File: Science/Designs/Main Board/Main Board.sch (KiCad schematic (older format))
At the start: 49 parts

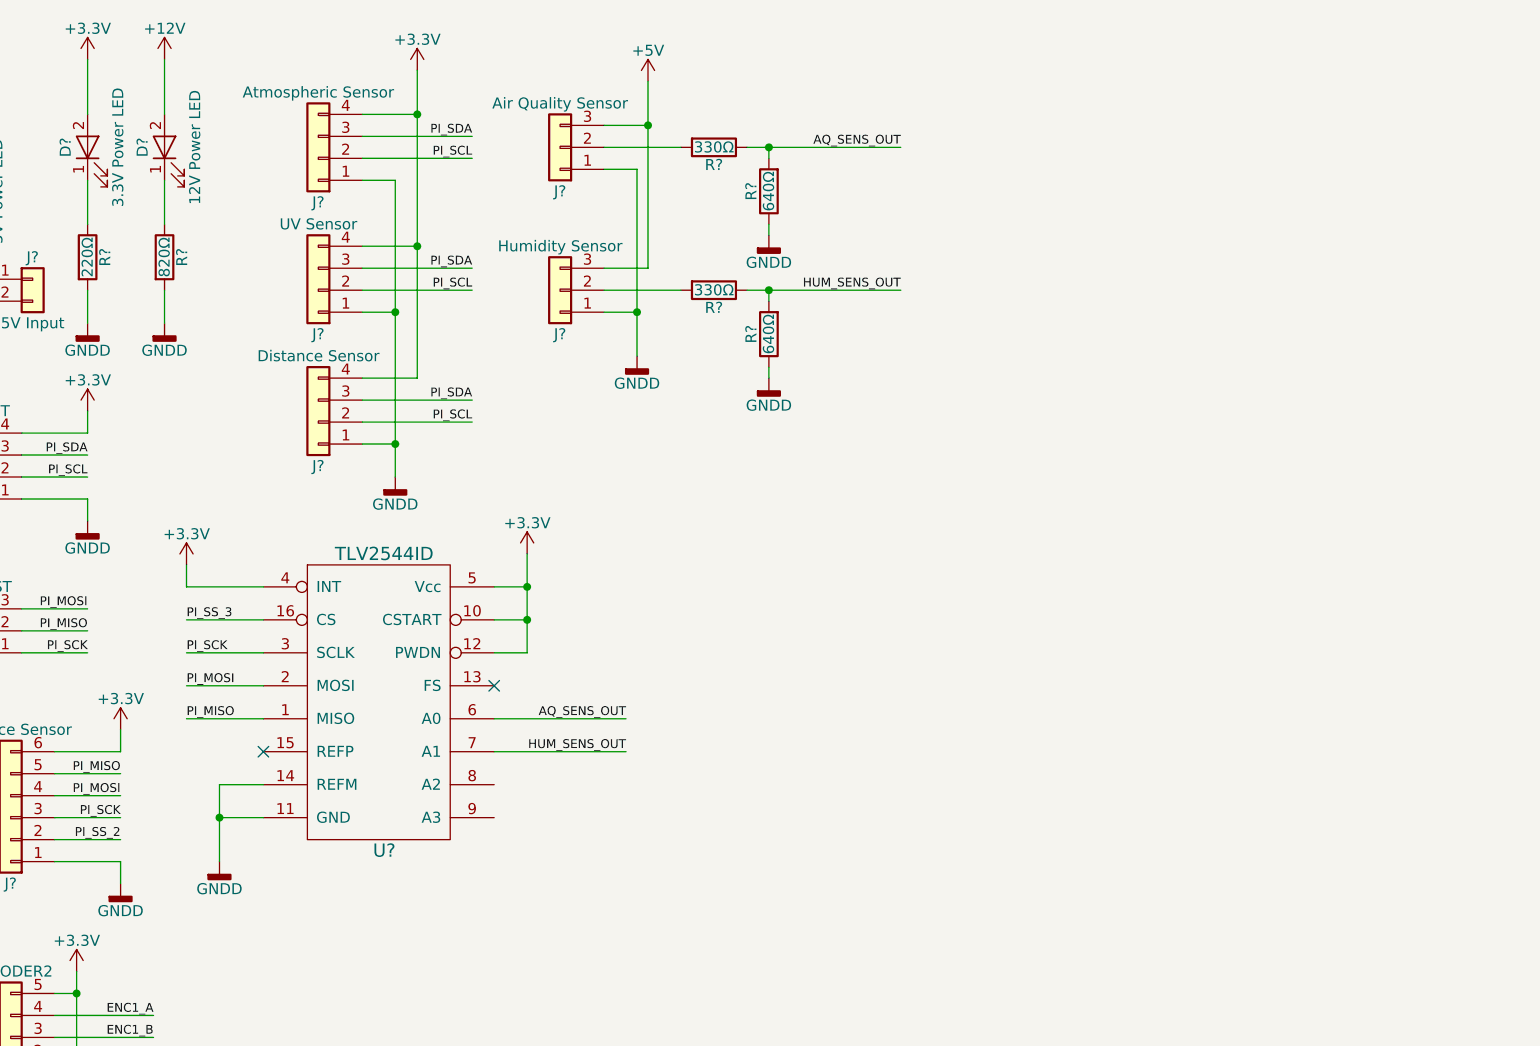
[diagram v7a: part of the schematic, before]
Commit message: Aded PWM device to schematic
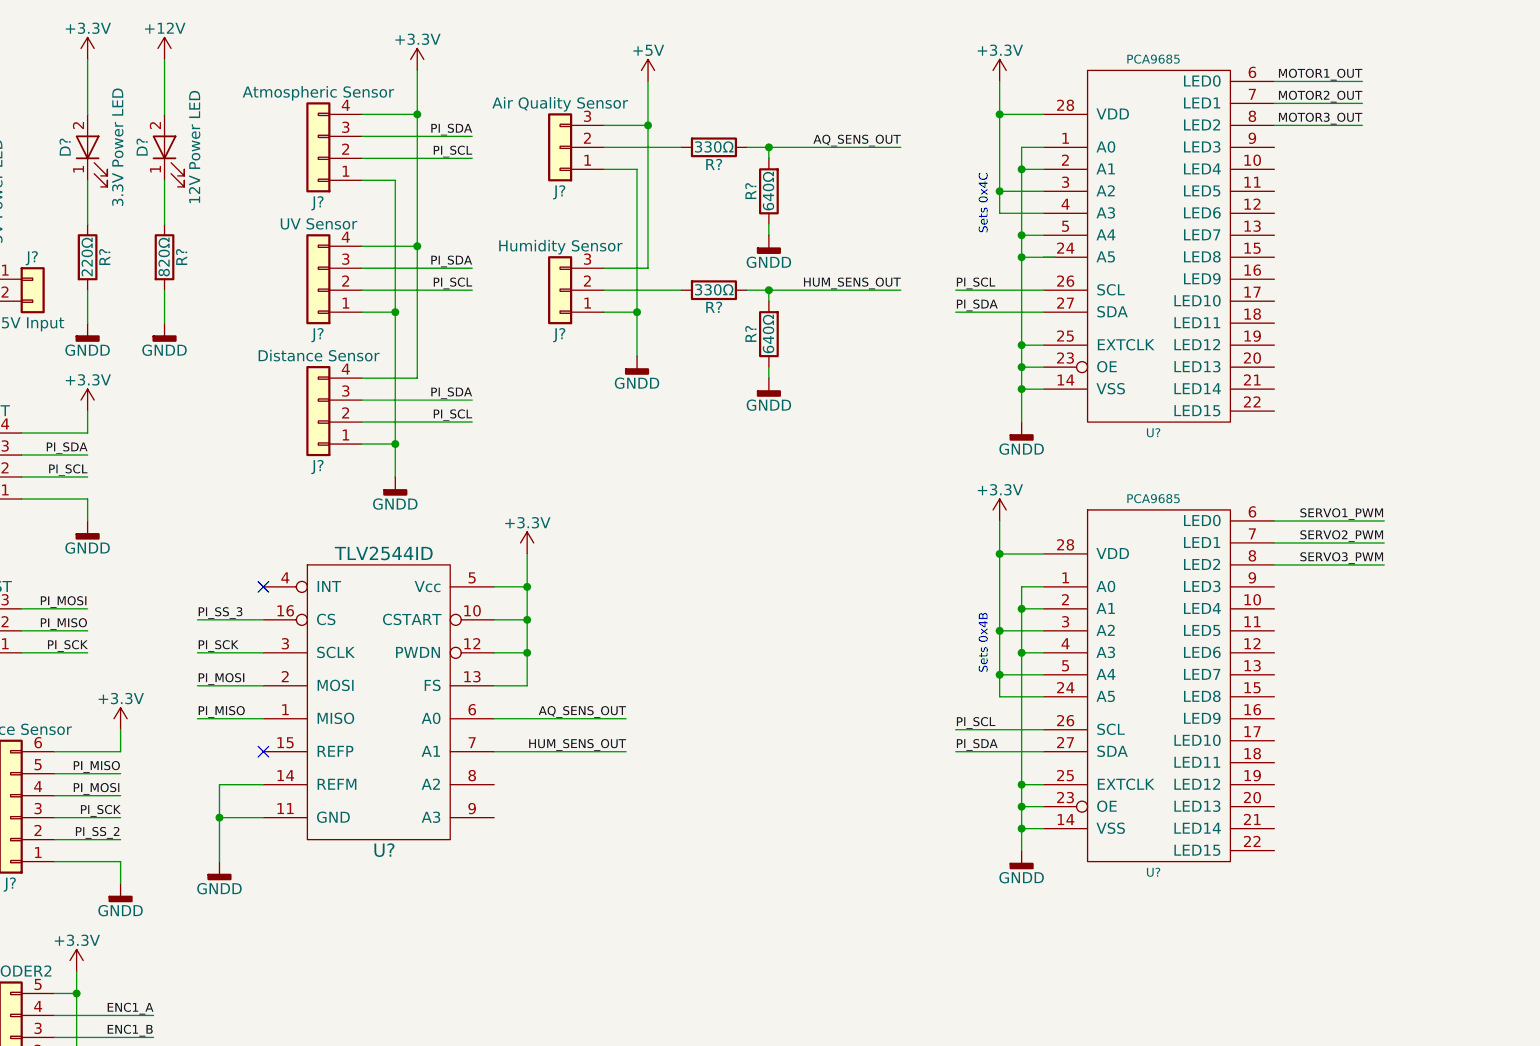
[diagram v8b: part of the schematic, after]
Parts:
- removed U?: TLV2544ID, symbol TLV2544ID
- added U?: TLV2544ID, symbol TLV2544ID
- added U? (x2): PCA9685, symbol PCA9685
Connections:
- net +3V3: now also U?.10 (CSTART), U?.12 (PWDN), U?.13 (FS), U?.24 (A5), U?.28 (VDD), U?.28 (VDD), U?.3 (A2), U?.3 (A2), U?.4 (A3), U?.5 (A4), U?.5 (Vcc)
- net AQ_SENS_OUT: now also U?.6 (A0)
- net GNDD: now also U?.1 (A0), U?.1 (A0), U?.11 (GND), U?.14 (REFM), U?.14 (VSS), U?.14 (VSS), U?.2 (A1), U?.2 (A1), U?.23 (OE), U?.23 (OE), U?.25 (EXTCLK), U?.25 (EXTCLK), U?.4 (A3), U?.5 (A4)
- net HUM_SENS_OUT: now also U?.7 (A1)
- net MOTOR1_OUT: now also U?.6 (LED0)
- net MOTOR2_OUT: now also U?.7 (LED1)
- net MOTOR3_OUT: now also U?.8 (LED2)
- net PI_MISO: now also U?.1 (MISO)
- net PI_MOSI: now also U?.2 (MOSI)
- net PI_SCK: now also U?.3 (SCLK)
- net PI_SCL: now also U?.26 (SCL), U?.26 (SCL)
- net PI_SDA: now also U?.27 (SDA), U?.27 (SDA)
- net PI_SS_3: now also U?.16 (CS)
- net SERVO1_PWM: now also U?.6 (LED0)
- net SERVO2_PWM: now also U?.7 (LED1)
- net SERVO3_PWM: now also U?.8 (LED2)
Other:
- note added: "Sets 0x4B"
- note added: "Sets 0x4C"
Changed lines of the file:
@@
-$EndComp
-$Comp
-L TLV2544ID U?
-U 1 1 5A52817B
-P 2500 3800
-F 0 "U?" H 2500 3300 60  0000 C CNN
-F 1 "TLV2544ID" H 2500 4650 60  0000 C CNN
-F 2 "" H 2500 4650 60  0001 C CNN
-F 3 "" H 2500 4650 60  0001 C CNN
-	1    2500 3800
-	1    0    0    -1
 $EndComp
 $Comp
@@
 	1    0    0    -1
 $EndComp
-NoConn ~ 3000 3550
 NoConn ~ 1950 3850
-Text Label 1600 3400 0    40   ~ 0
+Text Label 1650 3400 0    40   ~ 0
 PI_SCK
-Text Label 1600 3550 0    40   ~ 0
+Text Label 1650 3550 0    40   ~ 0
 PI_MOSI
-Text Label 1600 3700 0    40   ~ 0
+Text Label 1650 3700 0    40   ~ 0
 PI_MISO
 $Comp
@@
 	3000 3100 3150 3100
 Wire Wire Line
-	3150 2950 3150 3400
+	3150 2950 3150 3550
 Wire Wire Line
 	1950 4150 1750 4150
@@
 Connection ~ 1750 4150
 Wire Wire Line
-	1950 3700 1600 3700
-Wire Wire Line
-	1950 3550 1600 3550
-Wire Wire Line
-	1950 3400 1600 3400
-Wire Wire Line
-	1950 3250 1600 3250
+	1950 3700 1650 3700
+Wire Wire Line
+	1950 3550 1650 3550
+Wire Wire Line
+	1950 3400 1650 3400
+Wire Wire Line
+	1950 3250 1650 3250
 Wire Wire Line
 	4150 1100 4850 1100
@@
 Text Label 9800 2300 0    40   ~ 0
 PI_SS_3
-Text Label 1600 3250 0    40   ~ 0
+Text Label 1650 3250 0    40   ~ 0
 PI_SS_3
-Wire Wire Line
-	1950 3100 1600 3100
-Wire Wire Line
-	1600 3100 1600 3000
+$Comp
+L TLV2544ID U?
+U 1 1 5A5313CE
+P 2500 3800
+F 0 "U?" H 2500 3300 60  0000 C CNN
+F 1 "TLV2544ID" H 2500 4650 60  0000 C CNN
+F 2 "" H 2500 4650 60  0001 C CNN
+F 3 "" H 2500 4650 60  0001 C CNN
+	1    2500 3800
+	1    0    0    -1
+$EndComp
+Wire Wire Line
+	3150 3550 3000 3550
+Connection ~ 3150 3400
+NoConn ~ 1950 3100
+$Comp
+L PCA9685 U?
+U 1 1 5A534637
+P 6000 3350
+F 0 "U?" H 6000 2300 40  0000 C CNN
+F 1 "PCA9685" H 6000 4000 40  0000 C CNN
+F 2 "" H 6000 2300 40  0001 C CNN
+F 3 "" H 6000 2300 40  0001 C CNN
+	1    6000 3350
+	1    0    0    -1
+$EndComp
+$Comp
+L PCA9685 U?
+U 1 1 5A5346EA
+P 6000 1350
+F 0 "U?" H 6000 300 40  0000 C CNN
+F 1 "PCA9685" H 6000 2000 40  0000 C CNN
+F 2 "" H 6000 300 40  0001 C CNN
+F 3 "" H 6000 300 40  0001 C CNN
+	1    6000 1350
+	1    0    0    -1
+$EndComp
+Wire Wire Line
+	5500 2000 5400 2000
+Wire Wire Line
+	5400 1100 5400 2350
+Wire Wire Line
+	5500 2200 5400 2200
+Connection ~ 5400 2200
+Wire Wire Line
+	5500 2100 5400 2100
+Connection ~ 5400 2100
+$Comp
+L GNDD #PWR?
+U 1 1 5A534CEC
+P 5400 2350
+F 0 "#PWR?" H 5400 2100 50  0001 C CNN
+F 1 "GNDD" H 5400 2225 50  0000 C CNN
+F 2 "" H 5400 2350 50  0001 C CNN
+F 3 "" H 5400 2350 50  0001 C CNN
+	1    5400 2350
+	1    0    0    -1
+$EndComp
+Wire Wire Line
+	5400 4000 5500 4000
+Wire Wire Line
+	5400 3100 5400 4300
+Wire Wire Line
+	5400 4200 5500 4200
+Connection ~ 5400 4200
+Wire Wire Line
+	5500 4100 5400 4100
+Connection ~ 5400 4100
+Wire Wire Line
+	5500 2950 5300 2950
+Wire Wire Line
+	5300 2800 5300 3600
+Wire Wire Line
+	5500 950  5300 950
+Wire Wire Line
+	5300 800  5300 1400
+$Comp
+L GNDD #PWR?
+U 1 1 5A5354B0
+P 5400 4300
+F 0 "#PWR?" H 5400 4050 50  0001 C CNN
+F 1 "GNDD" H 5400 4175 50  0000 C CNN
+F 2 "" H 5400 4300 50  0001 C CNN
+F 3 "" H 5400 4300 50  0001 C CNN
+	1    5400 4300
+	1    0    0    -1
+$EndComp
 $Comp
 L +3.3V #PWR?
-U 1 1 5A53104B
-P 1600 3000
-F 0 "#PWR?" H 1600 2850 50  0001 C CNN
-F 1 "+3.3V" H 1600 3140 50  0000 C CNN
-F 2 "" H 1600 3000 50  0001 C CNN
-F 3 "" H 1600 3000 50  0001 C CNN
-	1    1600 3000
-	1    0    0    -1
-$EndComp
+U 1 1 5A53555D
+P 5300 800
+F 0 "#PWR?" H 5300 650 50  0001 C CNN
+F 1 "+3.3V" H 5300 940 50  0000 C CNN
+F 2 "" H 5300 800 50  0001 C CNN
+F 3 "" H 5300 800 50  0001 C CNN
+	1    5300 800
+	1    0    0    -1
+$EndComp
+$Comp
+L +3.3V #PWR?
+U 1 1 5A53563D
+P 5300 2800
+F 0 "#PWR?" H 5300 2650 50  0001 C CNN
+F 1 "+3.3V" H 5300 2940 50  0000 C CNN
+F 2 "" H 5300 2800 50  0001 C CNN
+F 3 "" H 5300 2800 50  0001 C CNN
+	1    5300 2800
+	1    0    0    -1
+$EndComp
+Wire Wire Line
+	6550 800  6950 800
+Wire Wire Line
+	6550 900  6950 900
+Wire Wire Line
+	6550 1000 6950 1000
+Text Label 6950 800  2    40   ~ 0
+MOTOR1_OUT
+Text Label 6950 900  2    40   ~ 0
+MOTOR2_OUT
+Text Label 6950 1000 2    40   ~ 0
+MOTOR3_OUT
+Wire Wire Line
+	5500 1750 5100 1750
+Wire Wire Line
+	5500 1850 5100 1850
+Text Label 5100 1750 0    40   ~ 0
+PI_SCL
+Text Label 5100 1850 0    40   ~ 0
+PI_SDA
+Wire Wire Line
+	5500 3750 5100 3750
+Wire Wire Line
+	5500 3850 5100 3850
+Text Label 5100 3750 0    40   ~ 0
+PI_SCL
+Text Label 5100 3850 0    40   ~ 0
+PI_SDA
+Wire Wire Line
+	6550 2800 7050 2800
+Text Label 7050 2800 2    40   ~ 0
+SERVO1_PWM
+Wire Wire Line
+	6550 2900 7050 2900
+Text Label 7050 2900 2    40   ~ 0
+SERVO2_PWM
+Wire Wire Line
+	6550 3000 7050 3000
+Text Label 7050 3000 2    40   ~ 0
+SERVO3_PWM
+Wire Wire Line
+	5300 3600 5500 3600
+Connection ~ 5300 2950
+Wire Wire Line
+	5500 3500 5300 3500
+Connection ~ 5300 3500
+Wire Wire Line
+	5500 3300 5300 3300
+Connection ~ 5300 3300
+Wire Wire Line
+	5500 3100 5400 3100
+Connection ~ 5400 4000
+Wire Wire Line
+	5500 3200 5400 3200
+Connection ~ 5400 3200
+Wire Wire Line
+	5500 3400 5400 3400
+Connection ~ 5400 3400
+Text Notes 5250 3500 1    40   ~ 0
+Sets 0x4B
+Wire Wire Line
+	5300 1400 5500 1400
+Connection ~ 5300 950
+Wire Wire Line
+	5500 1300 5300 1300
+Connection ~ 5300 1300
+Wire Wire Line
+	5500 1100 5400 1100
+Connection ~ 5400 2000
+Wire Wire Line
+	5500 1200 5400 1200
+Connection ~ 5400 1200
+Wire Wire Line
+	5500 1500 5400 1500
+Connection ~ 5400 1500
+Wire Wire Line
+	5550 1600 5400 1600
+Connection ~ 5400 1600
+Text Notes 5250 1500 1    40   ~ 0
+Sets 0x4C
 $EndSCHEMATC
